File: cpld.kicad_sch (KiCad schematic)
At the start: 9 parts, among them J2 Conn_01x06_Pin, U6 ATF1508AS-10AU100

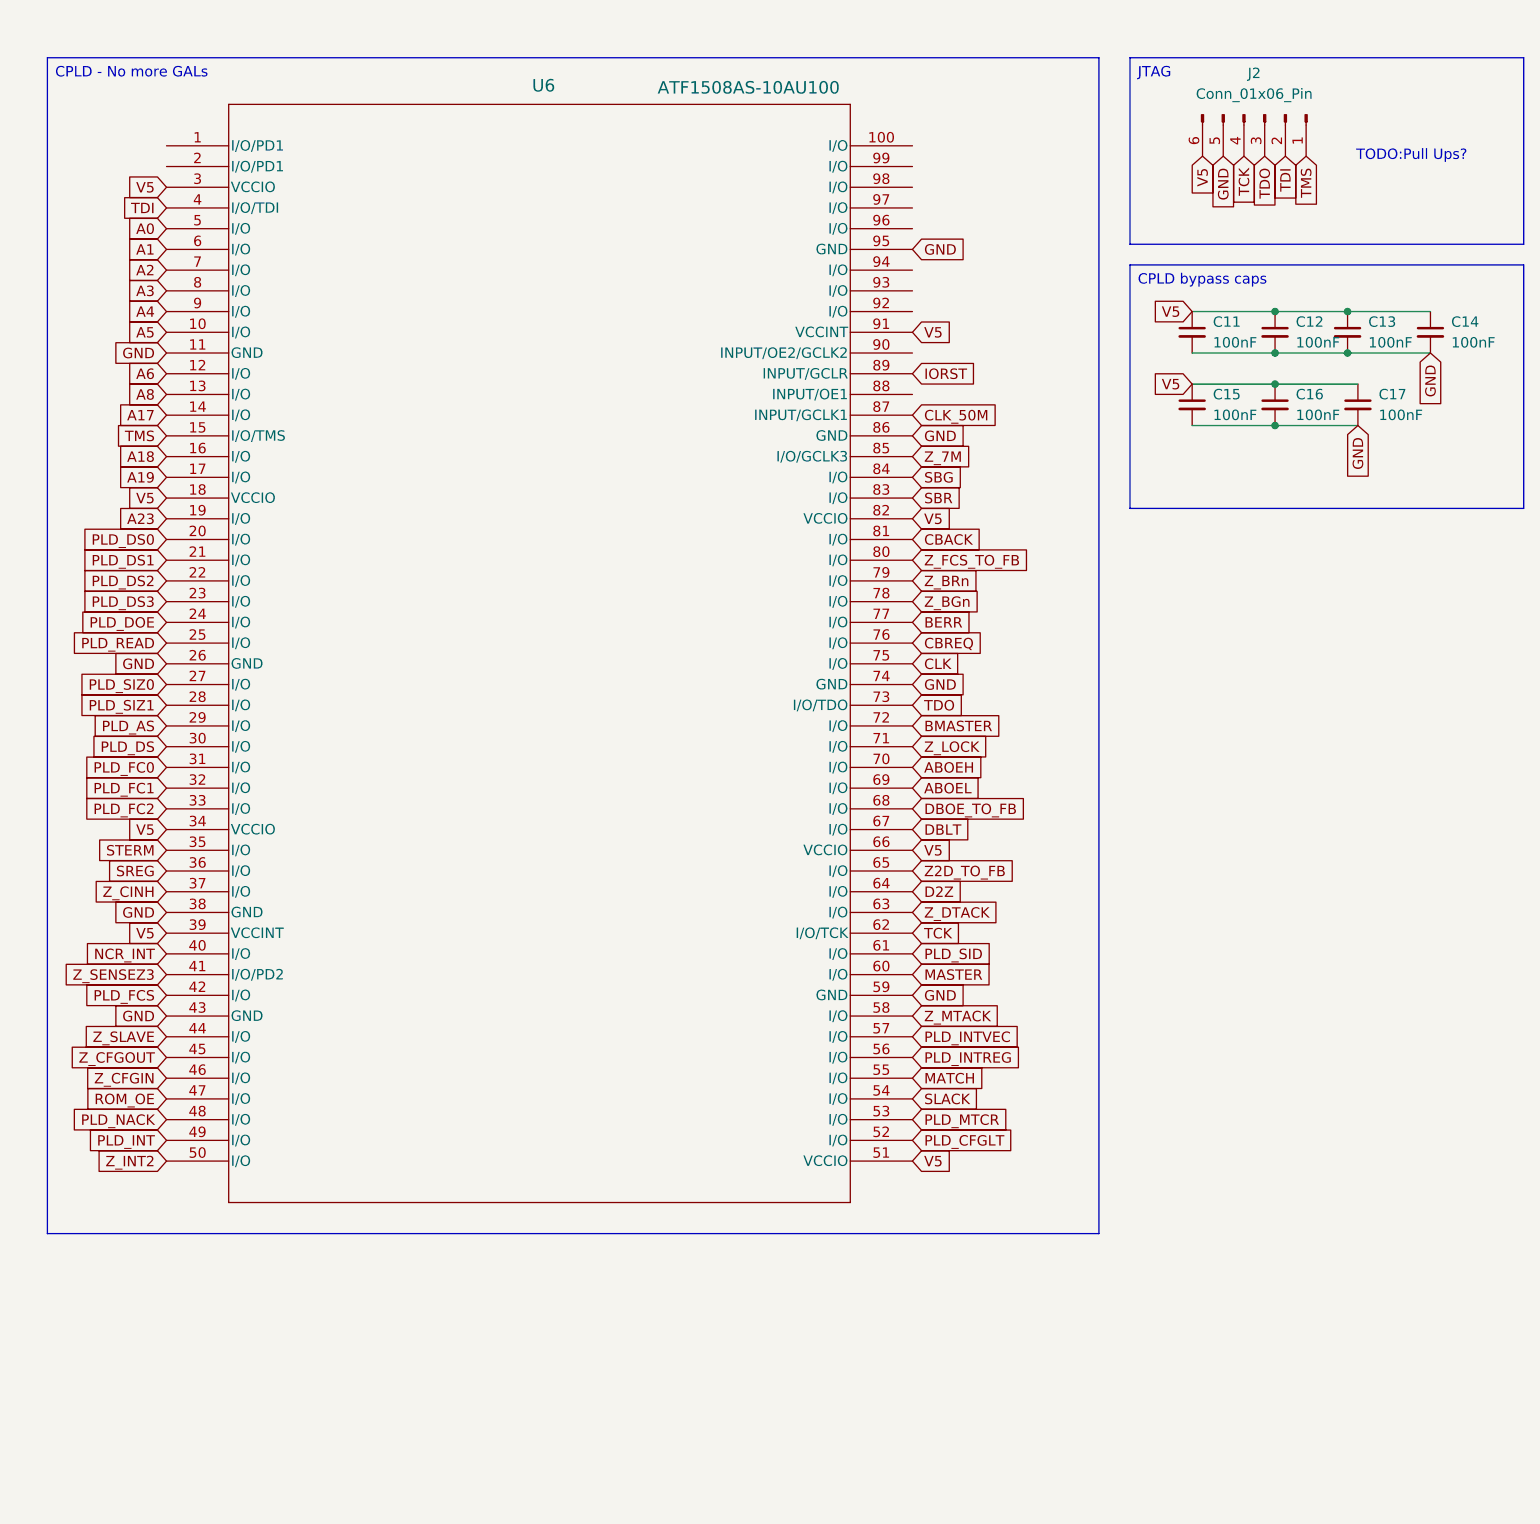
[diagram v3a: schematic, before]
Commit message: Move to XC95144XL
and other changes related to that.
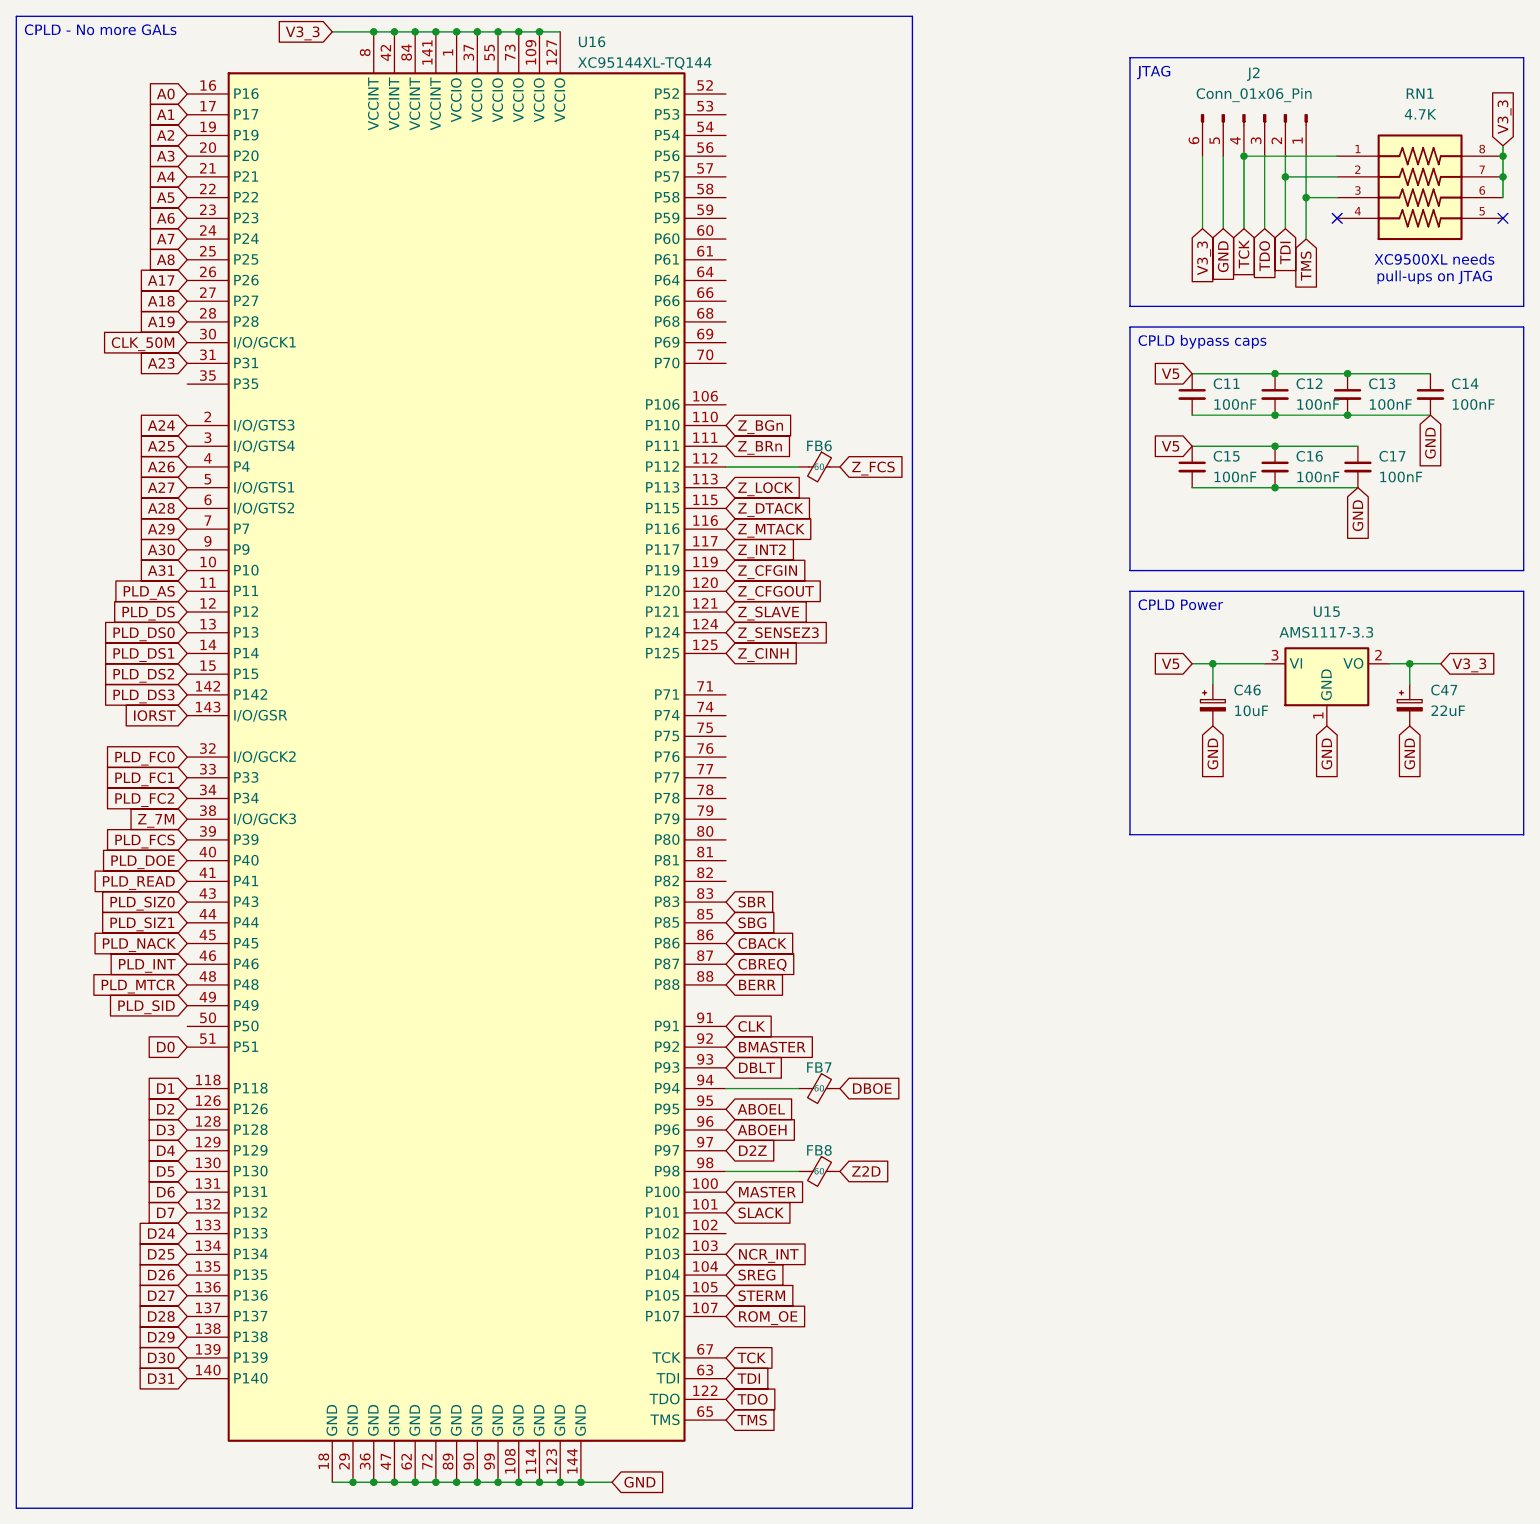
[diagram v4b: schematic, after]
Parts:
- removed U6: ATF1508AS-10AU100, ATF1508AS:100A_ATM, symbol ATF1508AS:ATF1508AS-10AU100
- added C46: 10uF, Capacitor_SMD:CP_Elec_6.3x7.7, symbol Device:C_Polarized_Small
- added C47: 22uF, Capacitor_SMD:CP_Elec_6.3x7.7, symbol Device:C_Polarized_Small
- added FB6, FB7, FB8: 60, Capacitor_SMD:C_0603_1608Metric_Pad1.08x0.95mm_HandSolder, symbol Device:FerriteBead_Small
- added RN1: 4.7K, YC324-FK-071KL:RESCAXS127P508X320X70-8N, symbol YC324-FK-071KL:YC324-FK-071KL
- added U15: AMS1117-3.3, Package_TO_SOT_SMD:SOT-223-3_TabPin2, symbol Regulator_Linear:AMS1117-3.3
- added U16: XC95144XL-TQ144, 144-TQFP_XIL, symbol CPLD_Xilinx:XC95144XL-TQ144
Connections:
- net A0: now also U16.16 (P16)
- net A1: now also U16.17 (P17)
- net A17: now also U16.26 (P26)
- net A18: now also U16.27 (P27)
- net A19: now also U16.28 (P28)
- net A2: now also U16.19 (P19)
- net A23: now also U16.31 (P31)
- net A3: now also U16.20 (P20)
- net A4: now also U16.21 (P21)
- net A5: now also U16.22 (P22)
- net A6: now also U16.23 (P23)
- net A8: now also U16.25 (P25)
- net ABOEH: now also U16.96 (P96)
- net ABOEL: now also U16.95 (P95)
- net BERR: now also U16.88 (P88)
- net BMASTER: now also U16.92 (P92)
- net CBACK: now also U16.86 (P86)
- net CBREQ: now also U16.87 (P87)
- net CLK: now also U16.91 (P91)
- net CLK_50M: now also U16.30 (I/O/GCK1)
- net D2Z: now also U16.97 (P97)
- net DBLT: now also U16.93 (P93)
- net GND: now also C46.2, C47.2, U15.1 (GND), U16.108 (GND), U16.114 (GND), U16.123 (GND), U16.144 (GND), U16.18 (GND), U16.29 (GND), U16.36 (GND), U16.47 (GND), U16.62 (GND), U16.72 (GND), U16.89 (GND), U16.90 (GND), U16.99 (GND)
- net IORST: now also U16.143 (I/O/GSR)
- net MASTER: now also U16.100 (P100)
- net NCR_INT: now also U16.103 (P103)
- net PLD_AS: now also U16.11 (P11)
- net PLD_DOE: now also U16.40 (P40)
- net PLD_DS: now also U16.12 (P12)
- net PLD_DS0: now also U16.13 (P13)
- net PLD_DS1: now also U16.14 (P14)
- net PLD_DS2: now also U16.15 (P15)
- net PLD_DS3: now also U16.142 (P142)
- net PLD_FC0: now also U16.32 (I/O/GCK2)
- net PLD_FC1: now also U16.33 (P33)
- net PLD_FC2: now also U16.34 (P34)
- net PLD_FCS: now also U16.39 (P39)
- net PLD_INT: now also U16.46 (P46)
- net PLD_MTCR: now also U16.48 (P48)
- net PLD_NACK: now also U16.45 (P45)
- net PLD_READ: now also U16.41 (P41)
- net PLD_SID: now also U16.49 (P49)
- net PLD_SIZ0: now also U16.43 (P43)
- net PLD_SIZ1: now also U16.44 (P44)
- net ROM_OE: now also U16.107 (P107)
- net SBG: now also U16.85 (P85)
- net SBR: now also U16.83 (P83)
- net SLACK: now also U16.101 (P101)
- net SREG: now also U16.104 (P104)
- net STERM: now also U16.105 (P105)
- net TCK: now also RN1.1, U16.67 (TCK)
- net TDI: now also RN1.2, U16.63 (TDI)
- net TDO: now also U16.122 (TDO)
- net TMS: now also RN1.3, U16.65 (TMS)
- net V5: now also C46.1, U15.3 (VI); no longer J2.6 (Pin_6)
- net Z_7M: now also U16.38 (I/O/GCK3)
- net Z_BGn: now also U16.110 (P110)
- net Z_BRn: now also U16.111 (P111)
- net Z_CFGIN: now also U16.119 (P119)
- net Z_CFGOUT: now also U16.120 (P120)
- net Z_CINH: now also U16.125 (P125)
- net Z_DTACK: now also U16.115 (P115)
- net Z_INT2: now also U16.117 (P117)
- net Z_LOCK: now also U16.113 (P113)
- net Z_MTACK: now also U16.116 (P116)
- net Z_SENSEZ3: now also U16.124 (P124)
- net Z_SLAVE: now also U16.121 (P121)
- new net: FB6.2, U16.112 (P112)
- new net: FB7.2, U16.94 (P94)
- new net: FB8.2, U16.98 (P98)
- new net A24: U16.2 (I/O/GTS3)
- new net A25: U16.3 (I/O/GTS4)
- new net A26: U16.4 (P4)
- new net A27: U16.5 (I/O/GTS1)
- new net A28: U16.6 (I/O/GTS2)
- new net A29: U16.7 (P7)
- new net A30: U16.9 (P9)
- new net A31: U16.10 (P10)
- new net A7: U16.24 (P24)
- new net D0: U16.51 (P51)
- new net D1: U16.118 (P118)
- new net D2: U16.126 (P126)
- new net D24: U16.133 (P133)
- new net D25: U16.134 (P134)
- new net D26: U16.135 (P135)
- new net D27: U16.136 (P136)
- new net D28: U16.137 (P137)
- new net D29: U16.138 (P138)
- new net D3: U16.128 (P128)
- new net D30: U16.139 (P139)
- new net D31: U16.140 (P140)
- new net D4: U16.129 (P129)
- new net D5: U16.130 (P130)
- new net D6: U16.131 (P131)
- new net D7: U16.132 (P132)
- new net DBOE: FB7.1
- new net V3_3: C47.1, J2.6 (Pin_6), RN1.6, RN1.7, RN1.8, U15.2 (VO), U16.1 (VCCIO), U16.109 (VCCIO), U16.127 (VCCIO), U16.141 (VCCINT), U16.37 (VCCIO), U16.42 (VCCINT), U16.55 (VCCIO), U16.73 (VCCIO), U16.8 (VCCINT), U16.84 (VCCINT)
- new net Z2D: FB8.1
- new net Z_FCS: FB6.1
- no-connect marks 0 -> 2
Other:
- note added: "XC9500XL needs pull-ups on JTAG"
- note removed: "TODO:Pull Ups?"
- moved on the sheet: C11, C12, C13, C14, C15, C16, C17
